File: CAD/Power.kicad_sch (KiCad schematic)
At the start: 81 parts, among them U10 AOZ1284, U14 TS30041, U18 AP7330-W5-7, U4 AP7361C-33E-13

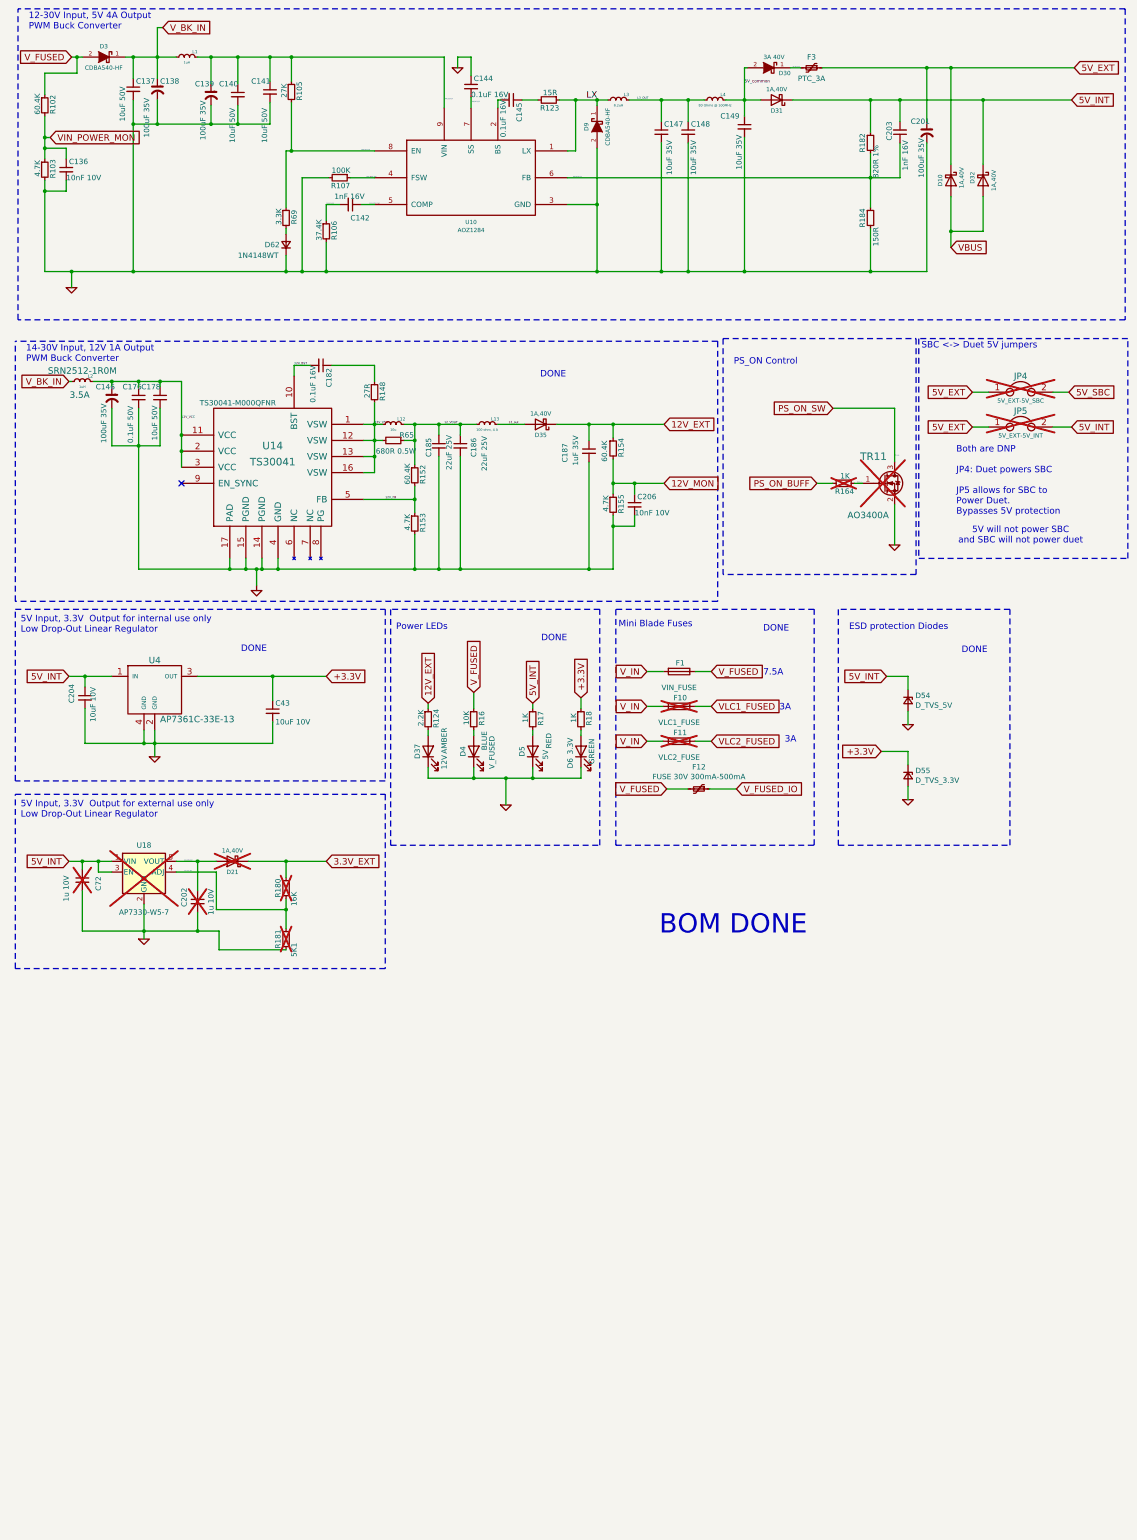
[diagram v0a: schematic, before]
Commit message: WIP redoing board for new print
Removed version resistors.
Added pull-up on CMD.
Working on motors, not routed.
Added local library for custom parts.
Ran auto-cleanup of traces and vias (supervised).
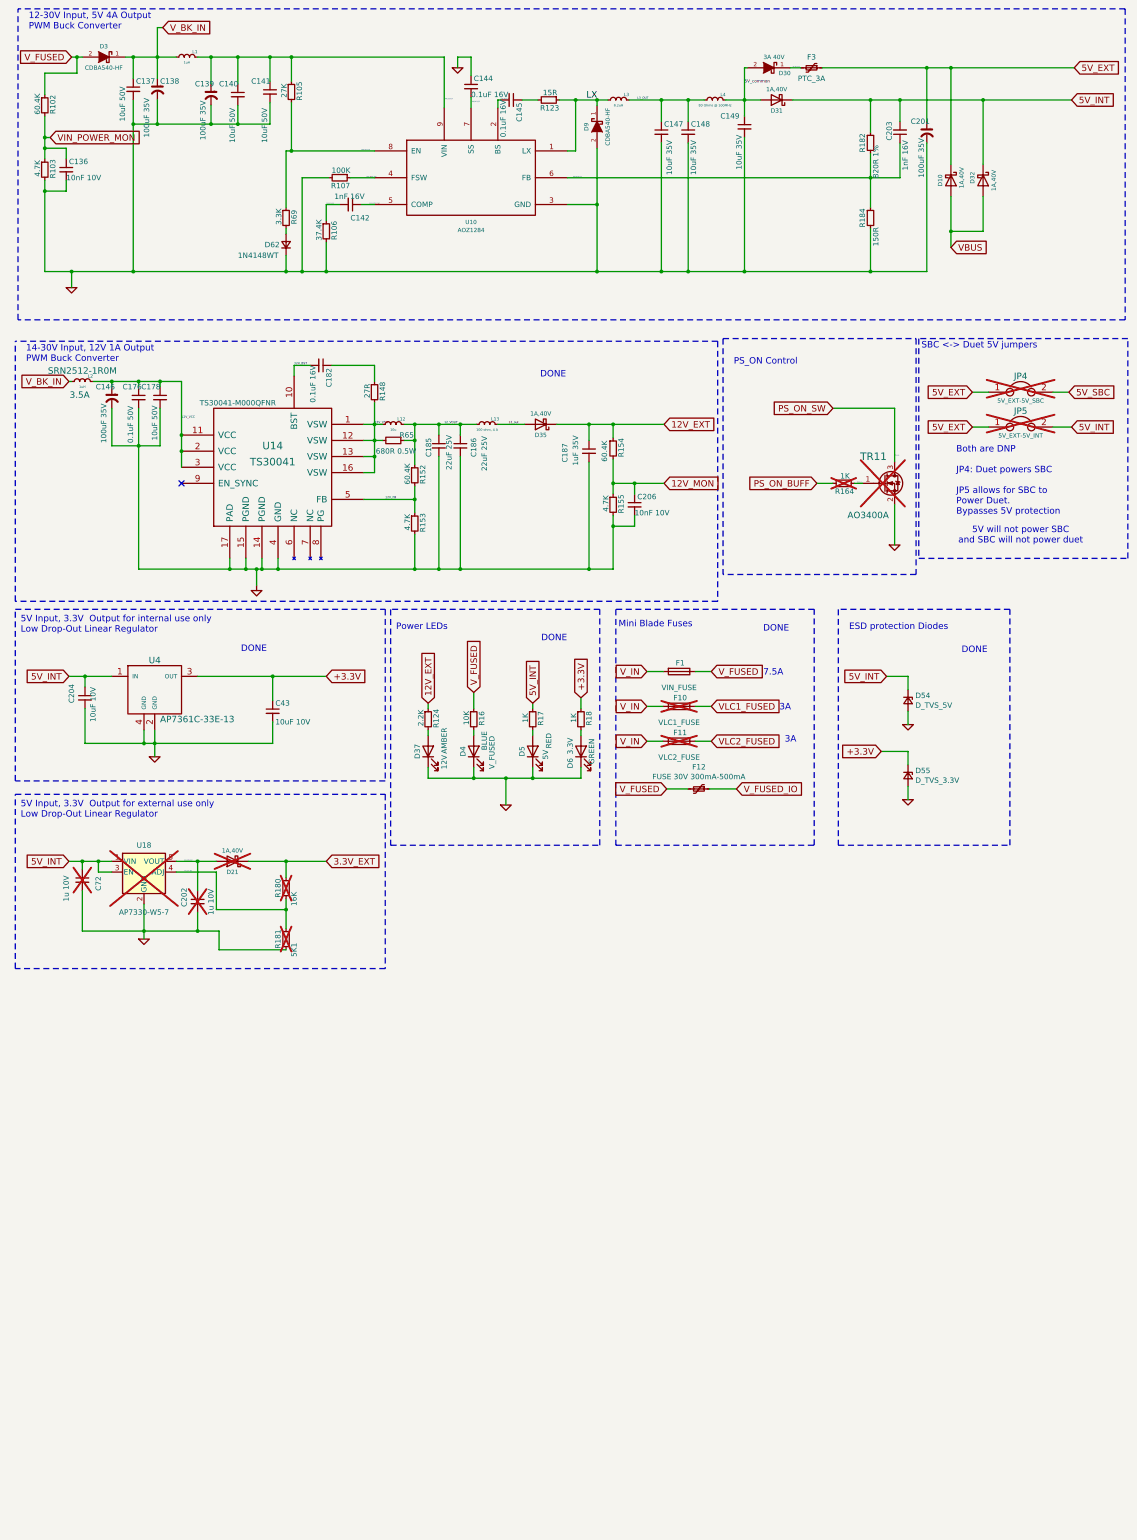
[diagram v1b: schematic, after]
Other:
- note removed: "BOM DONE"
- company: Duet3d -> 3DPotter
- title: Duet 3 Main Board 6XD -> Duet 3 Main Board 3DP
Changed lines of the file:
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@@
 (kicad_sch
-	(version 20231120)
+	(version 20250114)
 	(generator "eeschema")
-	(generator_version "8.0")
+	(generator_version "9.0")
 	(paper "A3" portrait)
 	(title_block
-		(title "Duet 3 Main Board 6XD")
+		(title "Duet 3 Main Board 3DP")
 		(date "2023-02-22")
-		(rev "1.01")
-		(company "Duet3d")
-		(comment 1 "(c) Duet3D")
+		(rev "1.0")
+		(company "3DPotter")
+		(comment 1 "(c) 3DPotter")
+	)
+	(text "Both are DNP\n\nJP4: Duet powers SBC\n\nJP5 allows for SBC to\nPower Duet.\nBypasses 5V protection"
+		(exclude_from_sim no)
+		(at 240.03 136.525 0)
+		(effects
+			(font
+				(size 1.524 1.524)
+			)
+			(justify left bottom)
+		)
+	)
+	(text "5V will not power SBC \nand SBC will not power duet"
+		(exclude_from_sim no)
+		(at 255.27 141.224 0)
+		(effects
+			(font
+				(size 1.524 1.524)
+			)
+		)
+	)
+	(text "PS_ON Control"
+		(exclude_from_sim no)
+		(at 187.325 100.965 0)
+		(effects
+			(font
+				(size 1.524 1.524)
+			)
+			(justify left bottom)
+		)
+	)
+	(text "DONE\n"
+		(exclude_from_sim no)
+		(at 73.66 168.148 0)
+		(effects
+			(font
+				(size 1.524 1.524)
+			)
+		)
+	)
+	(text "3A\n"
+		(exclude_from_sim no)
+		(at 199.39 190.5 0)
+		(effects
+			(font
+				(size 1.524 1.524)
+			)
+			(justify left bottom)
+		)
+	)
+	(text "Mini Blade Fuses"
+		(exclude_from_sim no)
+		(at 160.02 163.195 0)
+		(effects
+			(font
+				(size 1.524 1.524)
+			)
+			(justify left bottom)
+		)
+	)
+	(text "7.5A"
+		(exclude_from_sim no)
+		(at 194.31 174.625 0)
+		(effects
+			(font
+				(size 1.524 1.524)
+			)
+			(justify left bottom)
+		)
+	)
+	(text "5V Input, 3.3V  Output for external use only\nLow Drop-Out Linear Regulator"
+		(exclude_from_sim no)
+		(at 18.415 208.28 0)
+		(effects
+			(font
+				(size 1.524 1.524)
+			)
+			(justify left bottom)
+		)
+	)
+	(text "Power LEDs"
+		(exclude_from_sim no)
+		(at 107.315 163.83 0)
+		(effects
+			(font
+				(size 1.524 1.524)
+			)
+			(justify left bottom)
+		)
+	)
+	(text "ESD protection Diodes"
+		(exclude_from_sim no)
+		(at 214.63 163.83 0)
+		(effects
+			(font
+				(size 1.524 1.524)
+			)
+			(justify left bottom)
+		)
+	)
+	(text "DONE\n"
+		(exclude_from_sim no)
+		(at 244.348 168.402 0)
+		(effects
+			(font
+				(size 1.524 1.524)
+			)
+		)
+	)
+	(text "DONE\n"
+		(exclude_from_sim no)
+		(at 197.358 163.322 0)
+		(effects
+			(font
+				(size 1.524 1.524)
+			)
+		)
+	)
+	(text "3A\n"
+		(exclude_from_sim no)
+		(at 198.12 182.88 0)
+		(effects
+			(font
+				(size 1.524 1.524)
+			)
+			(justify left bottom)
+		)
+	)
+	(text "14-30V Input, 12V 1A Output\nPWM Buck Converter\n"
+		(exclude_from_sim no)
+		(at 19.685 100.33 0)
+		(effects
+			(font
+				(size 1.524 1.524)
+			)
+			(justify left bottom)
+		)
+	)
+	(text "5V Input, 3.3V  Output for internal use only\nLow Drop-Out Linear Regulator"
+		(exclude_from_sim no)
+		(at 18.415 164.465 0)
+		(effects
+			(font
+				(size 1.524 1.524)
+			)
+			(justify left bottom)
+		)
+	)
+	(text "DONE\n"
+		(exclude_from_sim no)
+		(at 144.78 165.608 0)
+		(effects
+			(font
+				(size 1.524 1.524)
+			)
+		)
+	)
+	(text "12-30V Input, 5V 4A Output\nPWM Buck Converter\n"
+		(exclude_from_sim no)
+		(at 20.32 21.59 0)
+		(effects
+			(font
+				(size 1.524 1.524)
+			)
+			(justify left bottom)
+		)
+	)
+	(text "SBC <-> Duet 5V jumpers"
+		(exclude_from_sim no)
+		(at 231.775 97.155 0)
+		(effects
+			(font
+				(size 1.524 1.524)
+			)
+			(justify left bottom)
+		)
+	)
+	(text "DONE\n"
+		(exclude_from_sim no)
+		(at 144.526 103.124 0)
+		(effects
+			(font
+				(size 1.524 1.524)
+			)
+		)
 	)
 	(junction
@@
 		)
 	)
-	(text "Both are DNP\n\nJP4: Duet powers SBC\n\nJP5 allows for SBC to\nPower Duet.\nBypasses 5V protection"
-		(exclude_from_sim no)
-		(at 240.03 136.525 0)
-		(effects
-			(font
-				(size 1.524 1.524)
-			)
-			(justify left bottom)
-		)
-	)
-	(text "5V will not power SBC \nand SBC will not power duet"
-		(exclude_from_sim no)
-		(at 255.27 141.224 0)
-		(effects
-			(font
-				(size 1.524 1.524)
-			)
-		)
-	)
-	(text "PS_ON Control"
-		(exclude_from_sim no)
-		(at 187.325 100.965 0)
-		(effects
-			(font
-				(size 1.524 1.524)
-			)
-			(justify left bottom)
-		)
-	)
-	(text "DONE\n"
-		(exclude_from_sim no)
-		(at 73.66 168.148 0)
-		(effects
-			(font
-				(size 1.524 1.524)
-			)
-		)
-	)
-	(text "3A\n"
-		(exclude_from_sim no)
-		(at 199.39 190.5 0)
-		(effects
-			(font
-				(size 1.524 1.524)
-			)
-			(justify left bottom)
-		)
-	)
-	(text "Mini Blade Fuses"
-		(exclude_from_sim no)
-		(at 160.02 163.195 0)
-		(effects
-			(font
-				(size 1.524 1.524)
-			)
-			(justify left bottom)
-		)
-	)
-	(text "BOM DONE\n"
-		(exclude_from_sim no)
-		(at 187.198 233.426 0)
-		(effects
-			(font
-				(size 4.572 4.572)
-			)
-		)
-	)
-	(text "7.5A"
-		(exclude_from_sim no)
-		(at 194.31 174.625 0)
-		(effects
-			(font
-				(size 1.524 1.524)
-			)
-			(justify left bottom)
-		)
-	)
-	(text "5V Input, 3.3V  Output for external use only\nLow Drop-Out Linear Regulator"
-		(exclude_from_sim no)
-		(at 18.415 208.28 0)
-		(effects
-			(font
-				(size 1.524 1.524)
-			)
-			(justify left bottom)
-		)
-	)
-	(text "Power LEDs"
-		(exclude_from_sim no)
-		(at 107.315 163.83 0)
-		(effects
-			(font
-				(size 1.524 1.524)
-			)
-			(justify left bottom)
-		)
-	)
-	(text "ESD protection Diodes"
-		(exclude_from_sim no)
-		(at 214.63 163.83 0)
-		(effects
-			(font
-				(size 1.524 1.524)
-			)
-			(justify left bottom)
-		)
-	)
-	(text "DONE\n"
-		(exclude_from_sim no)
-		(at 244.348 168.402 0)
-		(effects
-			(font
-				(size 1.524 1.524)
-			)
-		)
-	)
-	(text "DONE\n"
-		(exclude_from_sim no)
-		(at 197.358 163.322 0)
-		(effects
-			(font
-				(size 1.524 1.524)
-			)
-		)
-	)
-	(text "3A\n"
-		(exclude_from_sim no)
-		(at 198.12 182.88 0)
-		(effects
-			(font
-				(size 1.524 1.524)
-			)
-			(justify left bottom)
-		)
-	)
-	(text "14-30V Input, 12V 1A Output\nPWM Buck Converter\n"
-		(exclude_from_sim no)
-		(at 19.685 100.33 0)
-		(effects
-			(font
-				(size 1.524 1.524)
-			)
-			(justify left bottom)
-		)
-	)
-	(text "5V Input, 3.3V  Output for internal use only\nLow Drop-Out Linear Regulator"
-		(exclude_from_sim no)
-		(at 18.415 164.465 0)
-		(effects
-			(font
-				(size 1.524 1.524)
-			)
-			(justify left bottom)
-		)
-	)
-	(text "DONE\n"
-		(exclude_from_sim no)
-		(at 144.78 165.608 0)
-		(effects
-			(font
-				(size 1.524 1.524)
-			)
-		)
-	)
-	(text "12-30V Input, 5V 4A Output\nPWM Buck Converter\n"
-		(exclude_from_sim no)
-		(at 20.32 21.59 0)
-		(effects
-			(font
-				(size 1.524 1.524)
-			)
-			(justify left bottom)
-		)
-	)
-	(text "SBC <-> Duet 5V jumpers"
-		(exclude_from_sim no)
-		(at 231.775 97.155 0)
-		(effects
-			(font
-				(size 1.524 1.524)
-			)
-			(justify left bottom)
-		)
-	)
-	(text "DONE\n"
-		(exclude_from_sim no)
-		(at 144.526 103.124 0)
-		(effects
-			(font
-				(size 1.524 1.524)
-			)
-		)
-	)

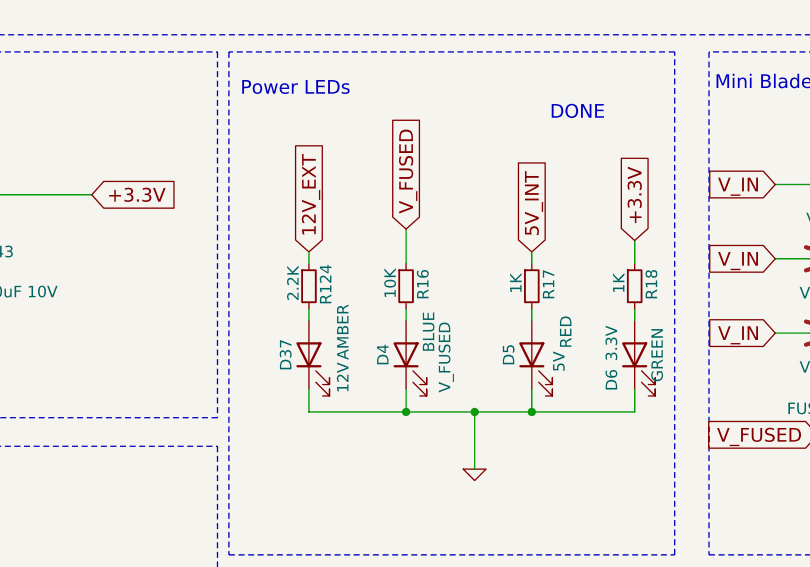
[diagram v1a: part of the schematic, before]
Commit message: update led resistors
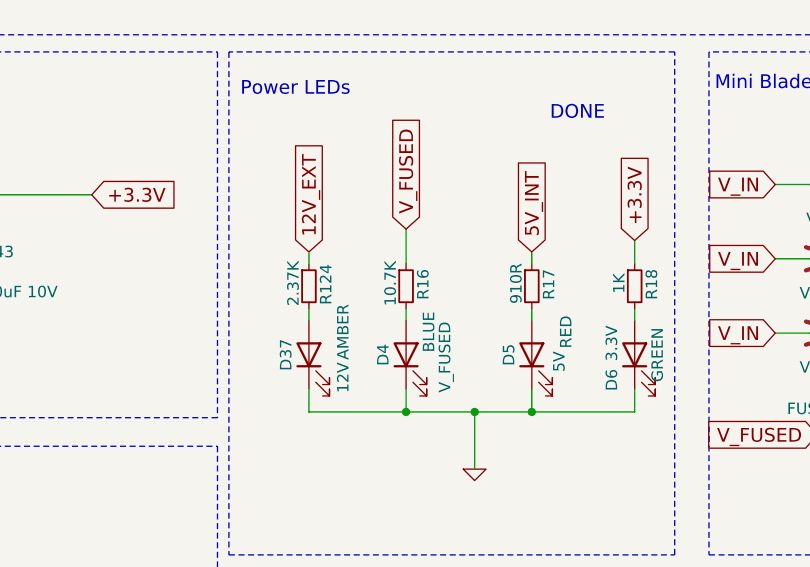
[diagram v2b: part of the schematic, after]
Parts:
- R124: value 2.2K -> 2.37K; LCSC C144773 -> C226957; Part Number AC0402FR-072K2L -> AC0402FR-072K37L
- R16: value 10K -> 10.7K; LCSC C144807 -> C226748; Part Number AC0402FR-0710KL -> AC0402FR-0710K7L; Rating 0.1W is more than fine, board doesn't get more than 50V!!! -> 50V, 62.5mW
- R17: value 1K -> 910R; LCSC C144789 -> C227272; Part Number AC0402FR-071KL -> AC0402FR-07910RL
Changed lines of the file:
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@@
 			)
 		)
-		(property "Value" "10K"
+		(property "Value" "10.7K"
 			(at 124.0028 184.4802 90)
 			(effects
@@
 			)
 		)
-		(property "Part Number" "AC0402FR-0710KL"
+		(property "Part Number" "AC0402FR-0710K7L"
 			(at 125.73 184.785 0)
 			(effects
@@
 			)
 		)
-		(property "Rating" "0.1W is more than fine, board doesn't get more than 50V!!!"
+		(property "Rating" "50V, 62.5mW"
 			(at 125.73 184.785 0)
 			(effects
@@
 			)
 		)
-		(property "LCSC" "C144807"
+		(property "LCSC" "C226748"
 			(at 125.73 184.785 90)
 			(effects
@@
 			)
 		)
-		(property "Value" "1K"
+		(property "Value" "910R"
 			(at 137.9728 184.4802 90)
 			(effects
@@
 			)
 		)
-		(property "Part Number" "AC0402FR-071KL"
+		(property "Part Number" "AC0402FR-07910RL"
 			(at 139.7 184.785 0)
 			(effects
@@
 			)
 		)
-		(property "LCSC" "C144789"
+		(property "LCSC" "C227272"
 			(at 139.7 184.785 90)
 			(effects
@@
 			)
 		)
-		(property "Value" "2.2K"
+		(property "Value" "2.37K"
 			(at 113.2078 184.4802 90)
 			(effects
@@
 			)
 		)
-		(property "Part Number" "AC0402FR-072K2L"
+		(property "Part Number" "AC0402FR-072K37L"
 			(at 114.935 184.785 0)
 			(effects
@@
 			)
 		)
-		(property "LCSC" "C144773"
+		(property "LCSC" "C226957"
 			(at 114.935 184.785 90)
 			(effects

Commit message: Add Alternative Part
YI321611G800-6R0T is a valid replacement for UPB321611T-800Y-N (L4)
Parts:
- L4: LCSC C280704 -> C20416201; Part Number UPB321611T-800Y-N -> UPB321611T-800Y-N(C280704) or YI321611G800-6R0T(C20416201) 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
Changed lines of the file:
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@@
 			)
 		)
-		(property "Part Number" "UPB321611T-800Y-N"
+		(property "Part Number" "UPB321611T-800Y-N(C280704) or YI321611G800-6R0T(C20416201) (if UPB unavailable)"
 			(at 182.88 38.1 0)
 			(effects
@@
 			)
 		)
-		(property "LCSC" "C280704"
+		(property "LCSC" "C20416201"
 			(at 182.88 38.1 0)
 			(effects
